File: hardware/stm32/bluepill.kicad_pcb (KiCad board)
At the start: 2 copper layers, 99.1 x 99.1 mm, 14 parts, among them J1 LCD, J2 SD Card, J3 Radio, J4 Inside, J5 Outside, U1 PC817, U2 24LC512, U3 bluepill, U4 PC817

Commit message: bluepill Schematics 0.99
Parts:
- removed R3: R_Small, Resistors_SMD:R_0603_HandSoldering
- added C1: 220u, Capacitors_THT:CP_Radial_D10.0mm_P3.50mm, F.Cu at (133.1, 50.3)
- added C10: 100n, Capacitors_SMD:C_0805, F.Cu at (103.9, 133.1)
- added C11: 10u, Capacitors_Tantalum_SMD:CP_Tantalum_Case-A_EIA-3216-18_Reflow, F.Cu at (91.2, 68.1)
- added C2: 100n, Capacitors_SMD:C_0805, F.Cu at (90.2, 128.5)
- added C3: 100n, Capacitors_SMD:C_0805, F.Cu at (90.4, 131.1)
- added C4: 100n, Capacitors_SMD:C_0805, F.Cu at (96.5, 128.0)
- added C5: 100n, Capacitors_SMD:C_0805, F.Cu at (96.3, 133.1)
- added C6: 100n, Capacitors_SMD:C_0805, F.Cu at (96.3, 130.6)
- added C7: 100n, Capacitors_SMD:C_0805, F.Cu at (103.9, 130.6)
- added C8: 10u, Capacitors_Tantalum_SMD:CP_Tantalum_Case-A_EIA-3216-18_Reflow, F.Cu at (126.0, 121.9)
- added C9: 10u, Capacitors_Tantalum_SMD:CP_Tantalum_Case-A_EIA-3216-18_Reflow, F.Cu at (122.9, 121.9)
- added J10: Screw_Terminal_01x02, TerminalBlock:TerminalBlock_bornier-2_P5.08mm, F.Cu at (141.0, 83.8)
- added J11: Screw_Terminal_01x02, TerminalBlock:TerminalBlock_bornier-2_P5.08mm, F.Cu at (141.0, 94.0)
- added J12: Screw_Terminal_01x02, TerminalBlock:TerminalBlock_bornier-2_P5.08mm, F.Cu at (141.0, 104.1)
- added J13: Screw_Terminal_01x02, TerminalBlock:TerminalBlock_bornier-2_P5.08mm, F.Cu at (141.0, 114.3)
- added J14: RTC, Pin_Headers:Pin_Header_Straight_1x06_Pitch2.54mm, F.Cu at (67.1, 111.3)
- added J15: Screw_Terminal_01x02, TerminalBlock:TerminalBlock_bornier-2_P5.08mm, F.Cu at (141.0, 124.5)
- added J16: Conn_01x02_Male, Pin_Headers:Pin_Header_Straight_1x02_Pitch2.54mm, F.Cu at (78.0, 123.7)
- added J17: ESP-01, Socket_Strips:Socket_Strip_Straight_2x04_Pitch2.54mm, F.Cu at (102.1, 69.6)
- added J18: USART1, Pin_Headers:Pin_Header_Straight_1x04_Pitch2.54mm, F.Cu at (84.1, 109.0)
- added J19: Buttons, Pin_Headers:Pin_Header_Straight_1x05_Pitch2.54mm, F.Cu at (84.3, 90.4)
- added J6: Screw_Terminal_01x02, TerminalBlock:TerminalBlock_bornier-2_P5.08mm, F.Cu at (141.0, 53.3)
- added J7: Conn_01x02, Connectors_JST:JST_EH_B02B-EH-A_02x2.50mm_Straight, F.Cu at (83.1, 43.9)
- added J8: Screw_Terminal_01x02, TerminalBlock:TerminalBlock_bornier-2_P5.08mm, F.Cu at (141.0, 63.5)
- added J9: Screw_Terminal_01x02, TerminalBlock:TerminalBlock_bornier-2_P5.08mm, F.Cu at (141.0, 73.7)
- added Q1: Q_NMOS_GSD, TO_SOT_Packages_SMD:SOT-23, F.Cu at (134.6, 58.9)
- added Q2: Q_NMOS_GSD, TO_SOT_Packages_SMD:SOT-23, F.Cu at (134.6, 69.1)
- added Q3: Q_NMOS_GSD, TO_SOT_Packages_SMD:SOT-23, F.Cu at (134.6, 79.2)
- added Q4: Q_NMOS_GSD, TO_SOT_Packages_SMD:SOT-23, F.Cu at (134.6, 89.4)
- added Q5: Q_NMOS_GSD, TO_SOT_Packages_SMD:SOT-23, F.Cu at (134.6, 99.6)
- added Q6: Q_NMOS_GSD, TO_SOT_Packages_SMD:SOT-23, F.Cu at (134.6, 110.2)
- added R10: 470, Resistors_SMD:R_0603_HandSoldering, F.Cu at (124.0, 93.5)
- added R11: 470, Resistors_SMD:R_0603_HandSoldering, F.Cu at (124.0, 103.6)
- added R12: 470, Resistors_SMD:R_0603_HandSoldering, F.Cu at (124.0, 114.3)
- added R13: 4.7k, Resistors_SMD:R_0603_HandSoldering, F.Cu at (132.1, 58.9)
- added R14: 4.7k, Resistors_SMD:R_0603_HandSoldering, F.Cu at (132.1, 69.1)
- added R15: 4.7k, Resistors_SMD:R_0603_HandSoldering, F.Cu at (132.1, 79.2)
- added R16: 4.7k, Resistors_SMD:R_0603_HandSoldering, F.Cu at (132.1, 89.4)
- added R17: 4.7k, Resistors_SMD:R_0603_HandSoldering, F.Cu at (132.1, 99.6)
- added R18: 4.7k, Resistors_SMD:R_0603_HandSoldering, F.Cu at (132.1, 110.2)
- added R19: 4.7k, Resistors_SMD:R_0603_HandSoldering, F.Cu at (134.6, 56.4)
- added R20: 4.7k, Resistors_SMD:R_0603_HandSoldering, F.Cu at (131.6, 65.5)
- added R21: 4.7k, Resistors_SMD:R_0603_HandSoldering, F.Cu at (131.6, 75.7)
- added R22: 4.7k, Resistors_SMD:R_0603_HandSoldering, F.Cu at (131.6, 85.9)
- added R23: 4.7k, Resistors_SMD:R_0603_HandSoldering, F.Cu at (131.6, 96.0)
- added R24: 4.7k, Resistors_SMD:R_0603_HandSoldering, F.Cu at (132.1, 106.7)
- added R6: 470, Resistors_SMD:R_0603_HandSoldering, F.Cu at (64.1, 47.6)
- added R7: 470, Resistors_SMD:R_0603_HandSoldering, F.Cu at (124.0, 63.0)
- added R8: 470, Resistors_SMD:R_0603_HandSoldering, F.Cu at (124.0, 73.2)
- added R9: 470, Resistors_SMD:R_0603_HandSoldering, F.Cu at (124.0, 83.3)
- added U10: PC817, Housings_DIP:DIP-4_W7.62mm, F.Cu at (122.4, 98.6)
- added U11: PC817, Housings_DIP:DIP-4_W7.62mm, F.Cu at (122.4, 109.2)
- added U12: LM1117-3.3, TO_SOT_Packages_SMD:SOT-223, F.Cu at (131.8, 121.9)
- added U5: PC817, Housings_DIP:DIP-4_W7.62mm, F.Cu at (59.1, 40.6)
- added U6: PC817, Housings_DIP:DIP-4_W7.62mm, F.Cu at (122.4, 57.9)
- added U7: PC817, Housings_DIP:DIP-4_W7.62mm, F.Cu at (122.4, 68.1)
- added U8: PC817, Housings_DIP:DIP-4_W7.62mm, F.Cu at (122.4, 78.2)
- added U9: PC817, Housings_DIP:DIP-4_W7.62mm, F.Cu at (122.4, 88.4)
- R1, R2: value R_Small -> 4.7k
- R4, R5: value R_Small -> 470
- U1, U4: footprint Housings_SSOP:SOP-4_3.8x4.1mm_Pitch2.54mm -> Housings_DIP:DIP-4_W7.62mm_LongPads
- moved R4 30.6 mm to (101.6, 61.0)
- moved R5 30.6 mm to (101.6, 55.9)
- moved U1 30.6 mm to (95.2, 59.7)
- moved U4 30.6 mm to (95.2, 54.6)
- moved J5 29.8 mm to (106.7, 52.1)
- moved J4 29.8 mm to (106.7, 61.0)
- moved J1 29.6 mm to (55.9, 91.4)
- moved U2 29.6 mm to (55.9, 78.7)
- moved J3 29.6 mm to (49.5, 61.0)
- moved R2 28.4 mm to (77.5, 87.6)
- moved R1 26.5 mm to (80.0, 87.6)
- moved U3 5.40 mm to (100.6, 97.5)
- moved J2 4.89 mm to (117.1, 92.2)
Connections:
- J2 pad 6: +5V -> +3V3
- U3 pad 1: (no net) -> Net-(R6-Pad2)
- U3 pad 10: (no net) -> /MCU/BTN4
- U3 pad 14: (no net) -> /MCU/TX1
- U3 pad 15: (no net) -> /MCU/RX1
- U3 pad 18: +5V -> Net-(J16-Pad1)
- U3 pad 25: (no net) -> Net-(R12-Pad1)
- U3 pad 26: (no net) -> Net-(R11-Pad1)
- U3 pad 27: (no net) -> Net-(R10-Pad1)
- U3 pad 28: (no net) -> Net-(R9-Pad1)
- U3 pad 3: (no net) -> /MCU/LOOP_O
- U3 pad 33: (no net) -> Net-(R8-Pad1)
- U3 pad 34: (no net) -> Net-(R7-Pad1)
- U3 pad 35: /MCU/LOOP_I -> /MCU/ESP_RX
- U3 pad 36: /MCU/LOOP_O -> /MCU/ESP_TX
- U3 pad 4: (no net) -> /MCU/LOOP_I
- U3 pad 7: (no net) -> /MCU/BTN1
- U3 pad 8: (no net) -> /MCU/BTN2
- U3 pad 9: Net-(R3-Pad2) -> /MCU/BTN3
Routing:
- net +12V: track 0.00 -> 143.4 mm
- net GNDPWR: track 0.00 -> 95.5 mm, vias 0 -> 6
- net +3V3: track 0.00 -> 82.4 mm, vias 0 -> 2
- net GND: track 0.00 -> 19.4 mm
- net +5V: track 0.00 -> 16.5 mm
- net Net-(J13-Pad2): track 0.00 -> 5.77 mm
- net Net-(J10-Pad2): track 0.00 -> 5.56 mm
- net Net-(J9-Pad2): track 0.00 -> 5.56 mm
- net Net-(J8-Pad2): track 0.00 -> 5.56 mm
- net Net-(J12-Pad2): track 0.00 -> 5.56 mm
- net Net-(J11-Pad2): track 0.00 -> 5.56 mm
- net Net-(Q6-Pad1): track 0.00 -> 5.07 mm
- net Net-(Q3-Pad1): track 0.00 -> 5.07 mm
- net Net-(Q2-Pad1): track 0.00 -> 5.07 mm
- net Net-(Q1-Pad1): track 0.00 -> 5.07 mm
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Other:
- net class 3.3V added: clearance 0.2, trace_width 0.5, via_dia 0.6, via_drill 0.4
- net class 5V added: clearance 0.2, trace_width 0.5, via_dia 0.6, via_drill 0.4
- net class GND added: clearance 0.2, trace_width 0.5, via_dia 0.6, via_drill 0.4

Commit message: bluepill PCB progress
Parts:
- added C12: 100n, Capacitors_SMD:C_0805, F.Cu at (113.5, 123.4)
- added C13: 100n, Capacitors_SMD:C_0805, F.Cu at (106.2, 128.5)
- added D1: 1N4148, Diodes_SMD:D_MiniMELF, B.Cu at (143.5, 61.0)
- added D2: 1N4148, Diodes_SMD:D_MiniMELF, B.Cu at (143.5, 71.1)
- added D3: 1N4148, Diodes_SMD:D_MiniMELF, B.Cu at (143.5, 81.3)
- added D4: 1N4148, Diodes_SMD:D_MiniMELF, B.Cu at (143.5, 91.4)
- added D5: 1N4148, Diodes_SMD:D_MiniMELF, B.Cu at (143.5, 101.6)
- added D6: 1N4148, Diodes_SMD:D_MiniMELF, B.Cu at (143.5, 111.8)
- C10, C7, C8, C9, R10, R11, R12, R13, R14, R15, R16, R17, R18, R19, R20, R21, R22, R23, R24, R4, R5, R7, R8, R9, U12: moved to B.Cu
- J15: value Screw_Terminal_01x02 -> +5V
- Q1, Q2, Q3, Q4, Q5, Q6: value Q_NMOS_GSD -> IRLML2502; moved to B.Cu
- moved C7 68.1 mm to (127.0, 66.5), turned to 90 degrees
- moved J2 41.2 mm to (122.4, 133.1), turned to 90 degrees
- moved C2 41.2 mm to (49.0, 130.8)
- moved C4 39.7 mm to (56.9, 130.6)
- moved C3 37.3 mm to (53.1, 130.8)
- moved C5 35.7 mm to (60.7, 130.6)
- moved C11 31.8 mm to (121.2, 57.4), turned to 180 degrees
- moved C6 31.5 mm to (64.8, 130.6)
- moved R4 27.8 mm to (119.4, 39.6)
- moved J4 27.6 mm to (120.1, 36.8), turned to 270 degrees
- moved U1 26.3 mm to (115.3, 42.7), turned to 270 degrees
- moved C10 25.3 mm to (129.0, 130.6), turned to 180 degrees
- moved J17 23.6 mm to (119.9, 54.1), turned to 180 degrees
- moved U3 20.0 mm to (116.8, 85.9)
- moved R5 18.2 mm to (109.7, 39.6)
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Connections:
- J15 pad 1: +5V -> GND
- J15 pad 2: GND -> +5V
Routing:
- net +3V3: track 82.4 -> 148.7 mm, vias 2 -> 1
- net /MCU/MOSI: track 0.00 -> 62.7 mm, vias 0 -> 2
- net /MCU/MISO: track 0.00 -> 53.4 mm
- net /MCU/CS: track 0.00 -> 53.4 mm
- net /MCU/SCK: track 0.00 -> 52.4 mm
- net GND: track 19.4 -> 60.8 mm
- net /MCU/ESP_RX: track 0.00 -> 35.5 mm
- net /MCU/LOOP_O: track 0.00 -> 25.3 mm
- net /MCU/LOOP_I: track 0.00 -> 23.0 mm
- net Net-(R7-Pad1): track 0.00 -> 21.5 mm
- net /MCU/ESP_TX: track 0.00 -> 20.8 mm
- net +12V: track 143.4 -> 126.5 mm
- net Net-(R12-Pad1): track 0.00 -> 16.4 mm
- net Net-(R9-Pad1): track 0.00 -> 15.4 mm
- net Net-(R8-Pad1): track 0.00 -> 13.2 mm
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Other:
- board size 99.1 x 99.1 mm -> 100 x 100 mm
- net class 12V added: clearance 0.2, trace_width 2, via_dia 2, via_drill 0.8
- net class 3.3V: trace_width 0.5 -> 1
- net class 5V: trace_width 0.5 -> 1
- net class Default: trace_width 0.25 -> 0.254
- net class GND: trace_width 0.5 -> 1
- net class Strong added: clearance 0.2, trace_width 1, via_dia 0.6, via_drill 0.4

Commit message: bluepill: PCB 0.9
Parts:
- removed C13, C2: 100n, Capacitors_SMD:C_0805
- added R3: 1.8k, Resistors_SMD:R_0603_HandSoldering, B.Cu at (113.3, 83.3)
- added REF**: MountingHole_3.2mm_M3, Mounting_Holes:MountingHole_3.2mm_M3, F.Cu at (141.0, 39.0)
- added REF**: MountingHole_3.2mm_M3, Mounting_Holes:MountingHole_3.2mm_M3, F.Cu at (141.0, 131.0)
- added REF**: MountingHole_3.2mm_M3, Mounting_Holes:MountingHole_3.2mm_M3, F.Cu at (106.0, 131.0)
- added REF**: MountingHole_3.2mm_M3, Mounting_Holes:MountingHole_3.2mm_M3, F.Cu at (99.0, 57.0)
- C12, C4, R1, R2, R6: moved to B.Cu
- J18: footprint Pin_Headers:Pin_Header_Straight_1x04_Pitch2.54mm -> Pin_Headers:Pin_Header_Straight_1x03_Pitch2.54mm
- J4: value Inside -> Outer; footprint Pin_Headers:Pin_Header_Straight_1x03_Pitch2.54mm -> Pin_Headers:Pin_Header_Straight_1x02_Pitch2.54mm
- J5: value Outside -> Inner; footprint Pin_Headers:Pin_Header_Straight_1x03_Pitch2.54mm -> Pin_Headers:Pin_Header_Straight_1x02_Pitch2.54mm
- U5: footprint Housings_DIP:DIP-4_W7.62mm -> Housings_DIP:DIP-4_W7.62mm_LongPads
- moved C6 74.0 mm to (99.1, 65.0), turned to 90 degrees
- moved U2 68.8 mm to (107.2, 124.0), turned to 90 degrees
- moved J3 54.1 mm to (102.6, 68.6), turned to 180 degrees
- moved C3 52.4 mm to (104.4, 120.1), turned to 270 degrees
- moved C4 48.2 mm to (100.6, 110.2), turned to 270 degrees
- moved R1 48.0 mm to (114.8, 120.1)
- moved R2 48.0 mm to (112.3, 120.1)
- moved R6 45.1 mm to (108.2, 54.4)
- moved J1 42.8 mm to (97.0, 101.1), turned to 0 degrees
- moved U5 41.2 mm to (98.6, 50.3), turned to 90 degrees
- moved C5 39.4 mm to (100.1, 129.5), turned to 270 degrees
- moved J14 36.4 mm to (97.0, 131.1), turned to 180 degrees
- moved J16 31.5 mm to (103.6, 106.2), turned to 270 degrees
- moved J19 23.4 mm to (97.0, 71.1)
- moved J7 19.0 mm to (100.3, 37.3)
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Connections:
- U3 pad 10: /MCU/BTN4 -> /MCU/BTN1
- U3 pad 11: (no net) -> /MCU/BTN2
- U3 pad 12: (no net) -> /MCU/BTN3
- U3 pad 13: (no net) -> /MCU/BTN4
- U3 pad 7: /MCU/BTN1 -> (no net)
- U3 pad 8: /MCU/BTN2 -> (no net)
- U3 pad 9: /MCU/BTN3 -> /MCU/USB+
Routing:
- net GND: track 60.8 -> 217.5 mm, vias 0 -> 3
- net +5V: track 13.8 -> 130.3 mm, vias 0 -> 4
- net +3V3: track 148.7 -> 215.9 mm, vias 1 -> 2
- net /EEPROM/SDA: track 0.00 -> 52.4 mm, vias 0 -> 1
- net /EEPROM/SCL: track 0.00 -> 49.8 mm
- net /MCU/BTN1: track 0.00 -> 24.7 mm
- net /MCU/BTN2: track 0.00 -> 23.8 mm
- net /MCU/BTN3: track 0.00 -> 23.2 mm
- net /MCU/BTN4: track 0.00 -> 22.5 mm
- net Net-(J3-Pad2): track 0.00 -> 17.0 mm
- net /MCU/TX1: track 0.00 -> 14.1 mm
- net /MCU/RX1: track 0.00 -> 14.1 mm
- net Net-(R6-Pad2): track 0.00 -> 8.67 mm
- net /MCU/OPEN: track 0.00 -> 7.70 mm
- net Net-(J7-Pad1): track 0.00 -> 6.07 mm
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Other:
- board size 100 x 100 mm -> 50 x 100 mm
- net class 12V: clearance 0.2 -> 0.254
- net class 3.3V: clearance 0.2 -> 0.254
- net class 5V: clearance 0.2 -> 0.254
- net class Default: clearance 0.2 -> 0.2032
- net class GND: clearance 0.2 -> 0.254
- net class Strong: clearance 0.2 -> 0.254
- rule trace_clearance: 0.2 -> 0.2032

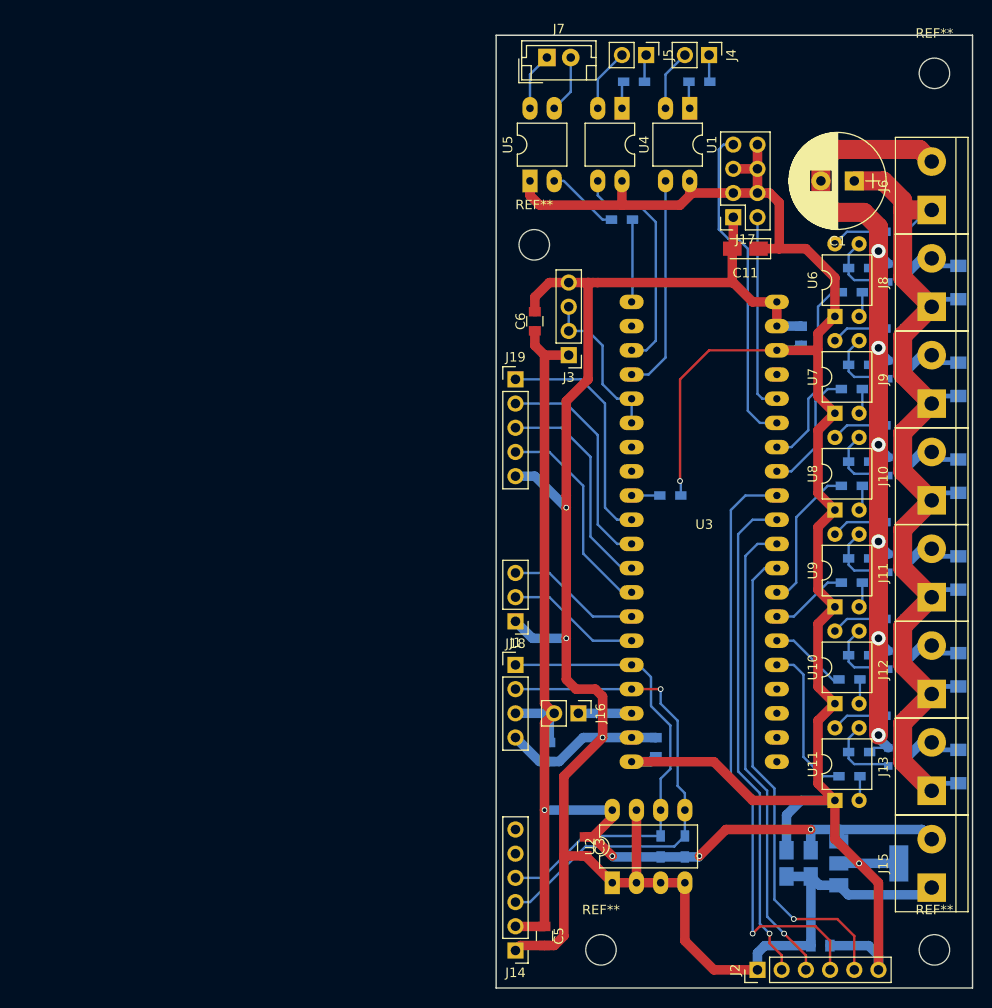
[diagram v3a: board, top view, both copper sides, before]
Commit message: bluepill PCB: SD Card socket turned around
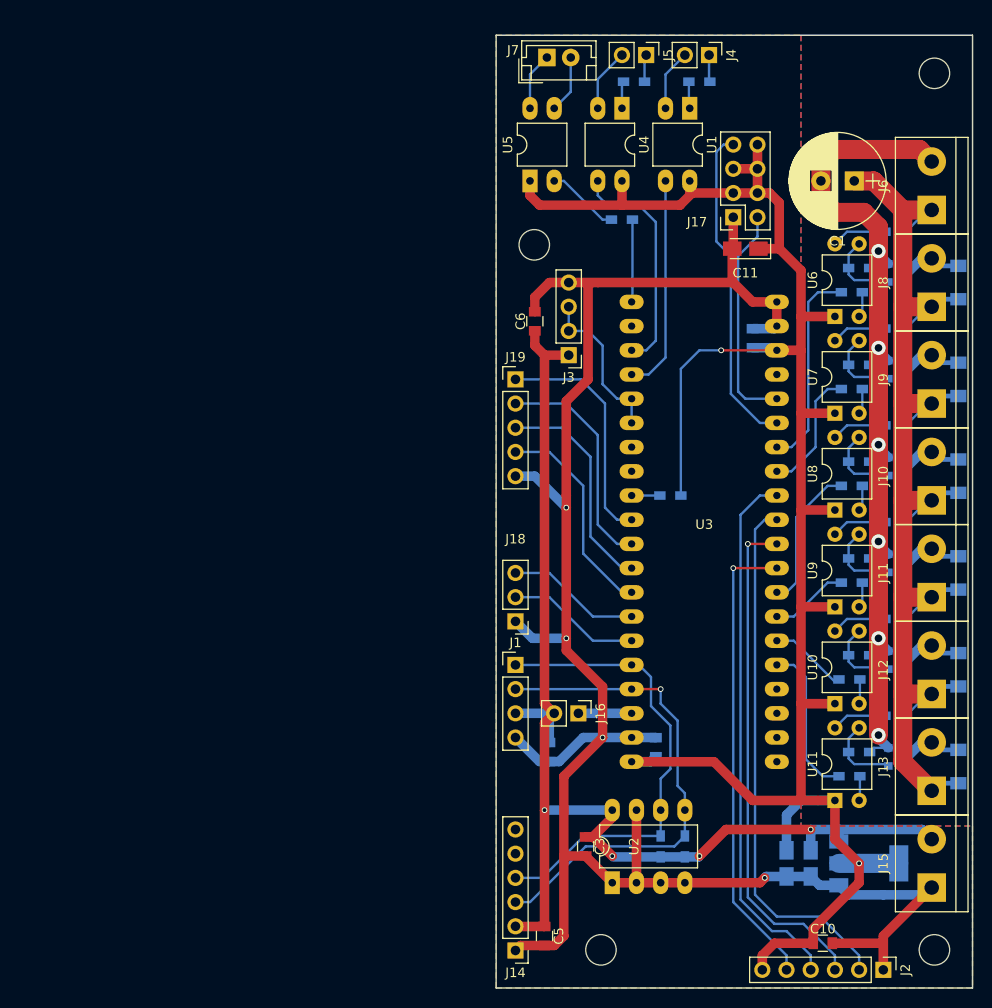
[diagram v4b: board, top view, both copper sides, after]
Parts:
- C10: moved to F.Cu
- J10: value Screw_Terminal_01x02 -> S3
- J11: value Screw_Terminal_01x02 -> S4
- J12: value Screw_Terminal_01x02 -> S5
- J13: value Screw_Terminal_01x02 -> S6
- J6: value Screw_Terminal_01x02 -> LED Power
- J7: value Conn_01x02 -> Open
- J8: value Screw_Terminal_01x02 -> S1
- J9: value Screw_Terminal_01x02 -> S2
- moved J2 13.2 mm to (135.6, 133.1), turned to 270 degrees
- moved C7 5.09 mm to (121.9, 66.8)
- moved C10 0.36 mm to (129.3, 130.3), turned to 0 degrees
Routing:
- net /MCU/MOSI: track 63.0 -> 56.3 mm, vias 1 -> 0
- net +3V3: track 215.9 -> 220.5 mm
- net GND: track 217.5 -> 213.5 mm, vias 3 -> 4
- net /MCU/MISO: track 52.3 -> 56.1 mm, vias 1 -> 0
- net /MCU/SCK: track 49.9 -> 53.3 mm
- net /MCU/ESP_TX: track 20.8 -> 23.5 mm
- net /MCU/CS: track 51.1 -> 49.1 mm
- net +12V: track 126.5 -> 127.5 mm
- net Net-(R7-Pad1): track 21.5 -> 22.4 mm
- net +5V: track 130.3 -> 129.8 mm
- added copper zone on B.Cu, net GND
- added copper zone on F.Cu, net GND

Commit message: bluepill-hardware: Final touches before manufacturing
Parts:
- moved U10 0.51 mm to (130.0, 105.2)
- moved U11 0.51 mm to (130.0, 115.3)
- moved U6 0.51 mm to (130.0, 64.5)
- moved U7 0.51 mm to (130.0, 74.7)
- moved U8 0.51 mm to (130.0, 84.8)
- moved U9 0.51 mm to (130.0, 95.0)
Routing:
- net +3V3: track 220.5 -> 217.2 mm
- net Net-(R19-Pad1): track 5.78 -> 6.70 mm
- net Net-(R24-Pad1): track 5.78 -> 6.28 mm
- net Net-(R23-Pad1): track 5.78 -> 6.28 mm
- net Net-(R22-Pad1): track 5.78 -> 6.28 mm
- net Net-(R21-Pad1): track 5.78 -> 6.28 mm
- net Net-(R20-Pad1): track 5.78 -> 6.28 mm
